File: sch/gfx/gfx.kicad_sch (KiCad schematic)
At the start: 104 parts

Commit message: schematic cleanups
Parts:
- removed R? (x2): 3k3, symbol AltDevice:R
- removed R?: 41k2, symbol AltDevice:R
- removed R?: 165k, symbol AltDevice:R
- removed U?: 74HC109, symbol AltDevice:74LS109
- removed U? (x2): 74HC02, symbol 74xx:74HC02
- removed U?: NE5532, symbol Amplifier_Operational:NE5532
- added C? (x3): 100n, symbol AltDevice:C
- added C?: 100u, symbol AltDevice:CP
- added C? (x2): 47u, symbol AltDevice:CP
- added D? (x2): 1N4148, symbol AltDevice:D
- added Q? (x2): 2N7000, symbol AltDevice:Q_NMOS_SGD
- added Q?: 2N3904, symbol AltDevice:Q_NPN_EBC
- added R5: 6k8, symbol AltDevice:R
- added R? (x2): 2k, symbol AltDevice:R
- added R?: 249k, symbol AltDevice:R
- added R?: 39, symbol AltDevice:R
- added R? (x4): 82k5, symbol AltDevice:R
- added R?: 499k, symbol AltDevice:R
- added RN?: 1k, Resistor_THT:R_Array_SIP9, symbol Device:R_Network08
- added unit 3 of U20
- added unit 4 of U6
- added unit 3 of U6
- D?: value 4148 -> 1N4148
- R?: Adjustment (none) -> HGAIN
- R?: Adjustment (none) -> VOFFSET
- R?: Adjustment (none) -> HOFFSET
- R?: Adjustment (none) -> VGAIN
- R?: value 1M -> 499k
- R?: value 1k -> 820
- R?: value 124k -> 249k
- RV?: renamed from R?; Adjustment (none) -> 4-6 SEP
- RV?: renamed from R?; Adjustment (none) -> FREQ
- RV?: renamed from R?; Adjustment (none) -> VSEP
- RV?: renamed from R?; Adjustment (none) -> 4-5 SEP
- U1: renamed from U?; value 74HC14 -> 'HC14; symbol 74xx:74HC14 -> AltDevice:74HC14
- U1: renamed from U?; value 74HC14 -> 'HC14
- U10: renamed from U?; value 74LS10 -> 'HC10
- U11, U12, U13, U9: renamed from U?; value 74HC161 -> 'HC161
- U14, U20, U7, U8: renamed from U?; value 74HC02 -> 'HC02
- U15: renamed from U?; value 74AHC244 -> 'AHC244
- U16, U17: renamed from U?; value 74HC273 -> 'HC273
- U2, U3, U4, U5: renamed from U?; value 74HC109 -> 'HC109
- U6: renamed from U?; value 74HC00 -> 'HC00
- gave numbers to parts that had none: 15
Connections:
- net +15V: now also C?.1, C?.1
- net +5V: now also U2.11 (S), U4.11 (S), U5.11 (S), C?.1, C?.1, Q?.3 (C), R?.2, R?.2, RN?.1 (common); no longer U2.5 (S), U4.5 (S), U4.5 (S), U5.5 (S)
- net -15V: now also C?.1, C?.2
- net CHAR0: now also U19.7 (A3); no longer U19.10 (A0)
- net CHAR1: now also U19.6 (A4); no longer U19.9 (A1)
- net CHAR2: now also U19.5 (A5); no longer U19.8 (A2)
- net CHAR3: now also U19.4 (A6); no longer U19.7 (A3)
- net CHAR4: now also U19.3 (A7); no longer U19.6 (A4)
- net CHAR5: now also U19.25 (A8); no longer U19.5 (A5)
- net CHARRSP0: now also RN?.2 (R1)
- net CHARRSP1: now also RN?.3 (R2)
- net CHARRSP2: now also RN?.4 (R3)
- net CHARRSP3: now also RN?.5 (R4)
- net CHARRSP4: now also RN?.6 (R5)
- net CHARRSP5: now also RN?.7 (R6)
- net CLK: now also U2.12 (C), U4.12 (C); no longer U2.4 (C), U4.4 (C)
- net DONE: now also U5.9 (Q); no longer U5.7 (Q)
- net DONEREQ: now also U7.5, U7.6; no longer U7.2, U7.3
- net GND: now also C?.1, C?.2, C?.2, C?.2, C?.2, C?.2, D?.2 (A), D?.2 (A), Q?.1 (S), Q?.1 (S), R5.1; no longer U14.3, U19.2 (A12)
- net HDOT0: now also U19.10 (A0), U6.5, R?.2; no longer R?.2, U19.4 (A6), U6.2
- net HDOT1: now also U19.9 (A1); no longer U19.3 (A7)
- net HDOT2: now also U19.8 (A2), U6.4; no longer U19.25 (A8), U6.1
- net LASTDOT: now also U8.4; no longer U8.1
- net LINE0: now also U19.21 (A10); no longer U19.24 (A9)
- net LINE1: now also U19.23 (A11); no longer U19.21 (A10)
- net LINE2: now also U19.2 (A12), R?.2; no longer U19.23 (A11)
- net POR: now also U2.9 (Q); no longer U2.7 (Q)
- net POS0: now also R?.2
- net POS2: now also R?.2, R?.2
- net POSCLK: now also U5.12 (C), R?.2; no longer U5.4 (C)
- net POSREQ0: now also U10.9; no longer U10.1
- net POSREQ1: now also U10.10; no longer U10.2
- net POSREQ2: now also U10.11; no longer U10.13
- net PREDONE: now also U14.12; no longer U14.3
- net RUN: now also U5.13 (K), U5.14 (J), U7.8; no longer U5.2 (J), U5.3 (K), U7.2
- net START: now also R5.2
- net ~DONE: now also U5.10 (Q); no longer U5.6 (Q)
- net ~LASTPOS: now also U10.8, U14.5, U14.6, U14.9; no longer U10.12
- net ~POR: now also U2.10 (Q), U4.15 (R); no longer U2.6 (Q), U4.1 (R), U4.1 (R)
- net ~RST: now also U1.6; no longer U1.2
- net ~RUN: now also U14.11, U20.6, U20.8; no longer U14.2, U20.2
- net V-: now reaches Q?.3 (C), R?.2
- net at C3.1, R?.1, R?.1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: now also D?.1 (K), R?.1, R?.1, R?.1, R?.1
- net at U12.10 (ENT): now also U14.4; no longer U14.1
- net at R4.2, U3.4 (C): now also U1.8; no longer U1.2
- net at U8.2: now also U6.6; no longer U6.3
- net H-: now reaches Q?.3 (C), R?.2
- net at C5.1, R?.1, R?.1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: now also D?.1 (K), R?.1, R?.1
- net at D?.1 (K), R3.2: now also U1.5; no longer U1.1
- net H+: now reaches Q?.3 (C), R?.1
- net at U13.10 (ENT): now also U14.10; no longer U14.1
- net at U7.3: now also U4.9 (Q); no longer U4.7 (Q)
- net at U20.1: now also U20.5; no longer U20.3
- net at C2.2, R2.1: now also U1.3; no longer U1.1
- net POSREQ'2: now reaches U15.14 (1Y2)
- net POSREQ'1: now reaches U15.16 (1Y1)
- net POSREQ'0: now reaches U15.18 (1Y0)
- net FLDREQ'0: now reaches U15.3 (2Y0)
- net FLDREQ'1: now reaches U15.5 (2Y1)
- net FLDREQ'2: now reaches U15.7 (2Y2)
- net at C?.1, RV?.1, RV?.2: now also U1.9; no longer U1.1
- net at U13.9 (~Pe): now also U14.13; no longer U14.1
- net V+: now reaches Q?.3 (C), R?.1
- net at R?.2: now also Q?.1 (E)
- removed net BLANK: U20.1
- net BRIGHT renamed ~INVERSE
- net ~INVERSE: now also U19.24 (A9)
- net BRIGHTRSP renamed ~INVRSP
- net ~INVRSP: now also RN?.8 (R7)
- net DIM renamed ~INTEN
- net ~INTEN: now also Q?.3 (D), U20.9
- net DIMRSP renamed ~INTENRSP
- net ~INTENRSP: now also RN?.9 (R8)
- net FIELD0 renamed FLD0
- net FIELD1 renamed FLD1
- net FIELD2 renamed FLD2
- net FLD2: now also Q?.2 (B)
- net FIELDREQ0 renamed FLDREQ0
- net FLDREQ0: now also U10.3; no longer U10.1
- net FIELDREQ1 renamed FLDREQ1
- net FLDREQ1: now also U10.4; no longer U10.2
- net FIELDREQ2 renamed FLDREQ2
- net FLDREQ2: now also U10.5; no longer U10.13
- removed net ~LASTFIELD: U10.12
- new net: R?.1, U6.11, U6.8
- new net: U6.10, U6.12, U6.13, U6.9, U8.1, U8.5, U8.6
- new net: U5.3 (K), U7.4, U7.9
- new net: U4.13 (K), U4.14 (J), U4.6 (Q)
- new net: Q?.2 (G), U20.4
- new net: R?.1, U1.10, U1.12
- new net: Q?.2 (G), U20.10
- new net: U1.11, U1.13, U3.6 (Q)
- new net: R?.1, R?.2 (x2)
- new net: U7.10, U7.11, U7.12
- new net: U5.15 (R), U7.13
- new net: U2.13 (K), U2.14 (J), U2.6 (Q)
- new net: U1.4, U2.1 (R), U2.15 (R)
- new net ~BLANK: Q?.3 (D)
- new net ~LASTFLD: U10.6, U14.8
- no-connect marks 12 -> 20
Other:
- note added: "0"
- note added: "0.5– 5mA"
- note added: "1"
- note added: "10µA"
- note added: "2"
- note added: "240µA"
- note added: "3"
- note added: "30µA"
- note added: "330µA"
- note added: "4"
- note added: "480µA"
- note added: "5"
- note added: "5µA"
- note added: "6"
- note added: "660µA"
- note added: "7"
- note added: "80µA"
- note added: "90µA"
- note added: "990µA"
- note added: "= virtual (B)lanking char, inserted for beam transit"
- note added: "B"
- note added: "HORIZONTAL DAC"
- note added: "J = START & DONE K = DONEREQ"
- note added: "OSD BUS"
- note added: "POSCLK lags CLK by one tP"
- note added: "Paper size is US Letter * 1.5, print scaled"
- note added: "SEQUENCE COUNTERS"
- note added: "Single cycle frame, START deasserted after fall of DONE"
- note added: "VERTICAL DAC"
- note removed: "(need to calculate)"
- note removed: "10µA per line 80µA per character box 0.5-5mA top-btm gap"
- note removed: "30µA per char"
- note removed: "5µA per dot"
- note removed: "Double flipflop stretches the transition to DONE, ensuring clean deactivation and reactivation."
- note removed: "FIELD4/5/6 SEPARATION"
- note removed: "GAP"
- note removed: "HOFFSET"
- note removed: "INTERFIELD BLANKING: In order to blank the beam while in transit between fields, a ninth virtual character is inserted at the end of every field. During this character, the beam is shut off. Due to the early increment of the field counter, this is simply visible to the external system as an extended prefetch of the first character of the next field."
- note removed: "J = START & !DONE K = DONEREQ"
- note removed: "POSCLK lags CLK by one tProp"
- note removed: "SYSTEM BUS"
- note removed: "Single cycle frame START deasserted after fall of DONE"
- note removed: "VGAIN"
- note removed: "VOFFSET"
- note removed: "dot = 5µA char width = 6; char = 30µA 8 chars per cell, cell = 240µA inter-cell space: 3 chars or 90µA cell with space: 330µA CELL0 CELL1 CELL2 CELL3 0µA 330µA 660µA 990µA 0µA 240µA480µA 990µA CELL4CELL5CELL6 CELL7"
- company: (none) -> Alexis Lockwood
- title: (none) -> OS2 On-screen display/graphics card

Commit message: Work in progress, not well organized, sorry
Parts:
- removed C?: 100p, symbol AltDevice:C
- removed R4: 6k8, symbol AltDevice:R
- removed R?: 39, symbol AltDevice:R
- removed RV?: 10k, symbol AltDevice:R_POT_TRIM
- removed unit 5 of U1
- removed unit 6 of U1
- removed U15: 'AHC244, symbol 74xx:74HC244
- removed U3: 'HC109, symbol AltDevice:74LS109
- removed U6: 'HC00, symbol 74xx:74HC00
- added R31: 499k, symbol AltDevice:R
- added R32: 249k, symbol AltDevice:R
- added U1: 1MHz, Oscillator:Oscillator_DIP-8, symbol Oscillator:CXO_DIP8
- added U15: 'AHC245, symbol 74xx:74LS245
- added unit 5 of U2
- added unit 6 of U2
- added unit 1 of U5
- added unit 1 of U6
- CD1: renamed from C?; value 100u -> 470µ
- CD2, CD41, CD44: renamed from C?; value 100n -> 1µ
- CD40, CD43: renamed from C?; value 47u -> 47µ
- R11, R12, R13, R14, R15: renamed from R?; value 82k5 -> 68k
- R28, R29, R43, R44: renamed from R?; symbol AltDevice:R -> AltDevice:R_HW
- R3: value 33k -> 10k
- R4: renamed from R?; value 39 -> 10
- U2: renamed from U1; symbol 74xx:74HC14 -> AltDevice:74HC14
- gave numbers to parts that had none: 45
- renumbered U14 to U10, U16 to U14, U17 to U16, U18 to U17, U19 to U18, U20 to U19, U1 to U2, U21 to U20, U22 to U21, U2 to U3, U9 to U4, U8 to U5, U10 to U6, U4 to U7, U5 to U8, U7 to U9
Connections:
- net +5V: now also U12.10 (ENT), U13.10 (ENT), U14.20 (VCC), U16.20 (VCC), U17.16 (VCC), U18.28 (VCC), U4.10 (ENT), U1.1 (EN), U1.8 (Vcc), U15.1 (A->B), U15.20 (VCC); no longer U12.7 (ENP), U13.7 (ENP), U4.7 (ENP)
- net CLK: now also U1.5 (OUT)
- net FLDREQ'0: now also U15.14 (B4)
- net FLDREQ'1: now also U15.13 (B5)
- net FLDREQ'2: now also U15.12 (B6)
- net FLDREQ0: now also U15.6 (A4)
- net FLDREQ1: now also U15.7 (A5)
- net FLDREQ2: now also U15.8 (A6)
- net GND: now also U14.10 (GND), U16.10 (GND), U17.8 (GND), U1.4 (GND), U15.10 (GND), U15.19 (CE), U15.5 (A3), U15.9 (A7)
- net HDOT0: now also U4.13 (Q1), U6.2; no longer U4.14 (Q0)
- net HDOT1: now also U4.12 (Q2), U5.9; no longer U4.13 (Q1), U5.3
- net HDOT2: now also U4.11 (Q3), U2.11, U2.13, U6.13; no longer U4.12 (Q2)
- net LASTDOT: now also U5.13; no longer U5.4
- net POR: now also U5.2
- net POSREQ'0: now also U15.18 (B0)
- net POSREQ'1: now also U15.17 (B1)
- net POSREQ'2: now also U15.16 (B2)
- net POSREQ0: now also U15.2 (A0)
- net POSREQ1: now also U15.3 (A1)
- net POSREQ2: now also U15.4 (A2)
- net RUN: no longer U4.10 (ENT)
- net ~POR: now also U7.1 (R); no longer U3.10 (Q)
- net ~RUN: now also U4.7 (ENP); no longer U10.11, U19.6, U19.8, U8.7 (Q)
- net at C5.1, D3.1 (K), R30.1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: now also R31.1, R32.1
- net at R4.1: now also U2.10, U2.12
- net at U10.4: now also U12.7 (ENP); no longer U12.10 (ENT)
- net RST#: now reaches U2.8
- net RST#: now also U11.1 (~MR), U12.1 (~MR), U13.1 (~MR), U4.1 (~MR)
- net at D1.2 (A), R3.1: now also U5.1
- net at U10.10: now also U13.7 (ENP); no longer U13.10 (ENT)
- net at U2.9: now also U2.6
- net DESCENDER0: now reaches U18.12 (D1)
- net DESCENDER0: now also R31.2
- net DESCENDER1: now reaches U18.13 (D2)
- net DESCENDER1: now also R32.2
- net ~BLANK renamed BLANK#
- net ~DONE renamed DONE#
- net ~INTEN renamed INTEN#
- net ~INTENRSP renamed INTENRSP#
- net ~INVERSE renamed CHAR6
- net ~INVRSP renamed CHARRSP6
- net ~LASTFLD renamed LASTFLD#
- net ~LASTPOS renamed LASTPOS#
- removed net ~RST: U11.1 (~MR), U12.1 (~MR), U13.1 (~MR), U2.6, U4.1 (~MR)
- new net: U4.14 (Q0), U6.1
- new net: U5.8, U6.12
- new net: U5.10, U5.11, U5.12
- new net POR#: U3.10 (Q)
- new net RUN#: U19.6, U19.8, U5.3, U8.7 (Q)
- no-connect marks 20 -> 17
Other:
- note added: "294µA"
- note added: "36µA"
- note added: "588µA"
- note added: "POSCLK lags CLK slightly"
- note added: "RST# lags CLK approximately 90°"
- note added: "hex: FNT1"
- note removed: "240µA"
- note removed: "480µA"
- note removed: "Adjust for fCLK = 500kHz (fosc = 1MHz)"
- note removed: "POSCLK lags CLK by one tP"
- note removed: "~RST~ lags CLK approximately 90°"

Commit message: blah blah
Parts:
- removed C4, C6: 100p, symbol AltDevice:C
- added R45, R46: 75, symbol AltDevice:R
- R24: value 5k1 -> 7k5
- R25, R30: value 2k -> 6k2
- R26, R41: value 150 -> 75
- R39: value 5k1 -> 3k
- RV4: value 10k -> 20k
- U14, U16: value 'HC273 -> 'AHCT273
- renumbered U22 to U21
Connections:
- net +15V: now also Q1.3 (C), R25.2, R30.2
- net +5V: now also R26.2, R41.2, R45.1, R46.1; no longer Q1.3 (C), R25.2, R30.2
- net GND: now also RV4.1, RV7.1, U21.3 (+), U21.5 (+); no longer U21.3 (+), U21.5 (+)
- net H-: now also R45.2; no longer R26.2
- net HDOT1: now also U5.6; no longer U5.9
- net LASTDOT: now also U5.1; no longer U5.13
- net POR: now also U5.11; no longer U5.2
- net RUN#: now also U10.11, U5.12; no longer U5.3
- net V-: now also R46.2; no longer R41.2
- net at Q7.2 (B): now also U21.1; no longer U21.7
- net at C5.1, D3.1 (K), R30.1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: now also R40.1, U21.6 (-); no longer RV5.3, U21.2 (-)
- net at D1.2 (A), R3.1: now also U5.13; no longer U5.1
- net at R38.2, R39.1: now also U21.2 (-); no longer U21.6 (-)
- net at R39.2, RV7.2: no longer RV7.1
- net at C5.2, Q6.2 (B): now also U21.7; no longer U21.1
- net at R24.2, RV4.2: no longer RV4.1
- net at U6.12: now also U5.5; no longer U5.8
- net at RV5.1, RV5.2: now also Q1.1 (E); no longer R40.1
- net at R40.2: now also RV5.3; no longer Q1.1 (E)
- new net: U5.2, U5.3, U5.4

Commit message: gfx board, pcb version
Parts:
- removed RN1: 1k, Resistor_THT:R_Array_SIP9, symbol Device:R_Network08
- added CD10, CD11, CD12, CD13, CD14, CD15, CD16, CD17, CD18, CD19, CD20, CD21, CD3, CD4, CD42, CD45, CD5, CD6, CD7, CD8, CD9: 1µ, Capacitor_SMD:C_0805_2012Metric_Pad1.15x1.40mm_HandSolder, symbol AltDevice:C
- added H1, H2: HOLE, MountingHole:MountingHole_3.2mm_M3_Pad_Via, symbol Connector:Conn_01x01_Male
- added P1: DIN41612_M_3x32, alt-libs:DIN41612_B_3x32_Horizontal, symbol AltConnector:DIN41612_M_3x32
- added RN1: 1k, Resistor_THT:R_Array_SIP10, symbol Device:R_Network09
- added unit 5 of U10
- added unit 5 of U19
- added unit 7 of U2
- added unit 3 of U20
- added unit 3 of U21
- added unit 3 of U3
- added unit 5 of U5
- added unit 4 of U6
- added unit 3 of U7
- added unit 3 of U8
- added unit 5 of U9
- C1, C2, C3, C5: footprint (none) -> Capacitor_THT:C_Disc_D4.7mm_W2.5mm_P5.00mm
- CD1: footprint (none) -> Capacitor_THT:CP_Radial_D8.0mm_P3.50mm; DKPN (none) -> 493-1743-ND
- CD2: footprint (none) -> Capacitor_SMD:C_0805_2012Metric_Pad1.15x1.40mm_HandSolder; Multiplier ×20 -> (none)
- CD40, CD43: footprint (none) -> Capacitor_THT:CP_Radial_D5.0mm_P2.00mm; DKPN (none) -> 493-1817-ND
- CD41, CD44: footprint (none) -> Capacitor_SMD:C_0805_2012Metric_Pad1.15x1.40mm_HandSolder; Multiplier ×2 -> (none)
- D1, D2, D3: footprint (none) -> Diode_THT:D_DO-35_SOD27_P10.16mm_Horizontal
- Q1, Q2, Q3, Q4, Q5, Q6, Q7: footprint (none) -> Package_TO_SOT_THT:TO-92
- R1, R10, R11, R12, R13, R14, R15, R16, R17, R18, R19, R2, R20, R21, R22, R23, R24, R25, R26, R27, R3, R30, R31, R32, R33, R34, R35, R36, R37, R38, R39, R4, R40, R41, R42, R45, R46, R5, R6, R7, R8, R9: footprint (none) -> Resistor_THT:R_Axial_DIN0207_L6.3mm_D2.5mm_P10.16mm_Horizontal
- R28, R29, R43, R44: footprint (none) -> Resistor_THT:R_Axial_DIN0309_L9.0mm_D3.2mm_P12.70mm_Horizontal
- RV1, RV2, RV3, RV4, RV5, RV6, RV7: footprint (none) -> alt-libs:stock_pot
- U10, U19, U2, U5, U6, U9: footprint (none) -> Package_DIP:DIP-14_W7.62mm
- U11, U12, U13, U3, U4, U7, U8: footprint (none) -> Package_DIP:DIP-16_W7.62mm
- U14, U15, U16: footprint (none) -> Package_DIP:DIP-20_W7.62mm
- U17: value 74HC237 -> 'HC237; footprint (none) -> Package_DIP:DIP-16_W7.62mm
- U18: footprint Package_DIP:DIP-28_W15.24mm -> Package_DIP:DIP-28_W15.24mm_Socket_LongPads
- U20, U21: footprint (none) -> Package_DIP:DIP-8_W7.62mm
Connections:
- net VCC is gone; now on net +5V: U11.16 (VCC), U12.16 (VCC), U13.16 (VCC), U4.16 (VCC)
- net ~RUN is gone; now on net RUN#: U4.7 (ENP)
- net +15V: now also CD42.1, P1.B28, U20.8 (V+), U21.8 (V+)
- net +5V: now also CD10.1, CD11.1, CD12.1, CD13.1, CD14.1, CD15.1, CD16.1, CD17.1, CD18.1, CD19.1, CD20.1, CD21.1, CD3.1, CD4.1, CD5.1, CD6.1, CD7.1, CD8.1, CD9.1, P1.A30, P1.A31, RN1.1 (common), U10.14 (VCC), U19.14 (VCC), U2.14 (VCC), U3.16 (VCC), U5.14 (VCC), U6.14 (VCC), U7.16 (VCC), U8.16 (VCC), U9.14 (VCC)
- net -15V: now also CD45.1, P1.B31, U20.4 (V-), U21.4 (V-)
- net GND: now also U21.3 (+), U21.5 (+), CD10.2, CD11.2, CD12.2, CD13.2, CD14.2, CD15.2, CD16.2, CD17.2, CD18.2, CD19.2, CD20.2, CD21.2, CD3.2, CD4.2, CD42.2, CD45.2, CD5.2, CD6.2, CD7.2, CD8.2, CD9.2, H1.1 (Pin_1), H2.1 (Pin_1), P1.A1, P1.A11, P1.A12, P1.A15, P1.A17, P1.A32, P1.A4, P1.A7, P1.A8, P1.B1, P1.B10, P1.B13, P1.B14, P1.B15, P1.B2, P1.B20, P1.B26, P1.B29, P1.B3, P1.B30, P1.B32, P1.B4, P1.B5, P1.B6, P1.B9, P1.C1, P1.C11, P1.C12, P1.C15, P1.C19, P1.C27, P1.C28, P1.C30, P1.C32, P1.C4, P1.C7, P1.C8, U10.7 (GND), U19.7 (GND), U2.7 (GND), U3.8 (GND), U5.7 (GND), U6.7 (GND), U7.8 (GND), U8.8 (GND), U9.7 (GND); no longer U21.3 (+), U21.5 (+)
- net INTEN#: no longer Q3.3 (D)
- net PREDONE: no longer R6.1, U10.2, U14.18 (D7)
- net at Q7.2 (B): now also U21.7; no longer U21.1
- net at C5.1, D3.1 (K), R30.1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: now also U21.2 (-); no longer U21.6 (-)
- net at R38.2, R39.1: now also U21.6 (-); no longer U21.2 (-)
- net at C5.2, Q6.2 (B): now also U21.1; no longer U21.7
- net BLANK# renamed A20
- net A20: now also P1.A20
- net CHARRSP0 renamed B22
- net B22: now also P1.B22, RN1.2 (R1)
- net CHARRSP1 renamed A22
- net A22: now also P1.A22, RN1.3 (R2)
- net CHARRSP2 renamed C23
- net C23: now also P1.C23, RN1.4 (R3)
- net CHARRSP3 renamed B23
- net B23: now also P1.B23, RN1.5 (R4)
- net CHARRSP4 renamed A23
- net A23: now also P1.A23, RN1.6 (R5)
- net CHARRSP5 renamed C24
- net C24: now also P1.C24, RN1.7 (R6)
- net CHARRSP6 renamed B24
- net B24: now also P1.B24, RN1.8 (R7)
- net DONE renamed A6
- net A6: now also P1.A6
- net FLDREQ'0 renamed B21
- net B21: now also P1.B21
- net FLDREQ'1 renamed A21
- net A21: now also P1.A21
- net FLDREQ'2 renamed C22
- net C22: now also P1.C22
- net H+ renamed A2
- net A2: now also P1.A2
- net H- renamed A3
- net A3: now also P1.A3
- net INTENRSP# renamed A24
- net A24: now also P1.A24, RN1.9 (R8)
- net POSREQ'0 renamed C25
- net C25: now also P1.C25
- net POSREQ'1 renamed B25
- net B25: now also P1.B25
- net POSREQ'2 renamed A25
- net A25: now also P1.A25
- net START renamed A5
- net A5: now also P1.A5
- net V+ renamed C2
- net C2: now also P1.C2
- net V- renamed C3
- net C3: now also P1.C3
- new net A10: P1.A10
- new net A13: P1.A13
- new net A14: P1.A14
- new net A16: P1.A16
- new net A18: P1.A18
- new net A19: P1.A19
- new net A26: P1.A26
- new net A27: P1.A27
- new net A28: P1.A28
- new net A29: P1.A29
- new net A9: P1.A9
- new net B11: P1.B11
- new net B12: P1.B12
- new net B16: P1.B16
- new net B17: P1.B17
- new net B18: P1.B18
- new net B19: P1.B19
- new net B27: P1.B27
- new net B7: P1.B7
- new net B8: P1.B8
- new net C10: P1.C10
- new net C13: P1.C13
- new net C14: P1.C14
- new net C16: P1.C16
- new net C17: P1.C17
- new net C18: P1.C18
- new net C20: P1.C20
- new net C21: P1.C21, Q3.3 (D)
- new net C26: P1.C26
- new net C29: P1.C29
- new net C31: P1.C31
- new net C5: P1.C5
- new net C6: P1.C6
- new net C9: P1.C9
- new net PREDONE': R6.1, U10.2, U14.18 (D7)
- no-connect marks 17 -> 18
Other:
- moved on the sheet: CD1, CD2, CD40, CD41, CD43, CD44

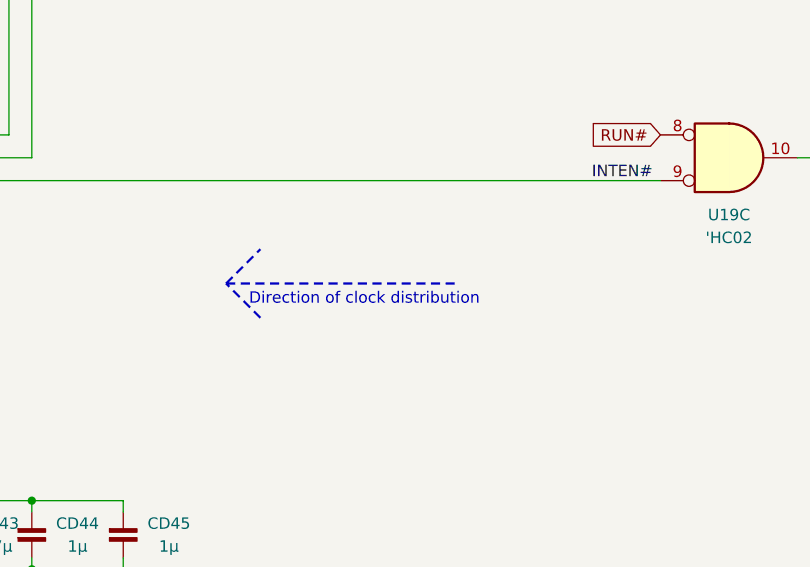
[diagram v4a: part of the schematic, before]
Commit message: gfx: sch adjustments and 3d models
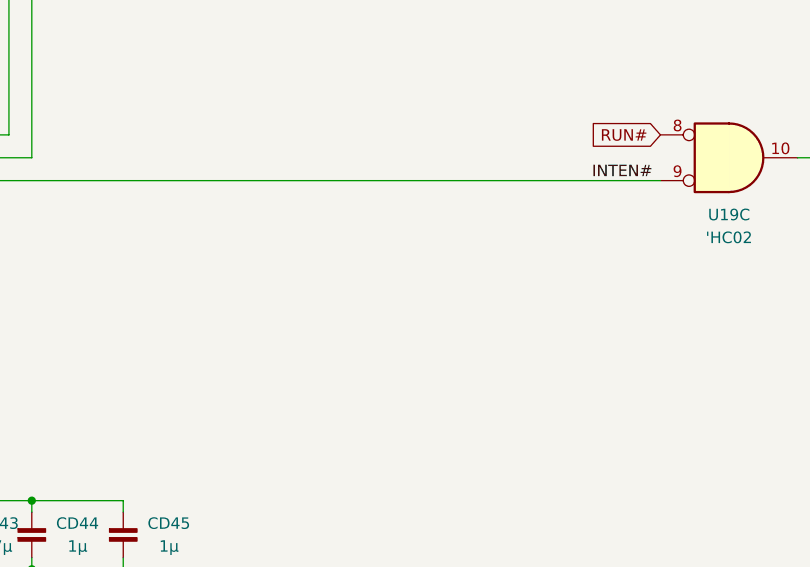
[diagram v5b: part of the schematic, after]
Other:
- note removed: "Direction of clock distribution"
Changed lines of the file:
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@@
-(kicad_sch (version 20200618) (host eeschema "(5.99.0-2039-g05a89863c)")
+(kicad_sch (version 20200618) (host eeschema "(5.99.0-2083-g40847c055)")
   (page 1 1)
   (paper "User" 419.1 323.85)
@@
   (junction (at 375.92 52.07) (diameter 0) (color 0 0 0 0))
   (junction (at 375.92 158.75) (diameter 0) (color 0 0 0 0))
-  (no_connect (at 264.16 99.06))
-  (no_connect (at 264.16 200.66))
-  (no_connect (at 151.13 205.74))
-  (no_connect (at 264.16 205.74))
-  (no_connect (at 264.16 88.9))
-  (no_connect (at 264.16 203.2))
+  (no_connect (at 88.9 231.14))
+  (no_connect (at 76.2 113.03))
+  (no_connect (at 53.34 118.11))
   (no_connect (at 99.06 246.38))
-  (no_connect (at 264.16 198.12))
   (no_connect (at 264.16 208.28))
-  (no_connect (at 76.2 113.03))
   (no_connect (at 64.77 35.56))
-  (no_connect (at 53.34 118.11))
-  (no_connect (at 88.9 231.14))
+  (no_connect (at 198.12 193.04))
+  (no_connect (at 264.16 198.12))
+  (no_connect (at 264.16 205.74))
+  (no_connect (at 151.13 205.74))
+  (no_connect (at 264.16 99.06))
+  (no_connect (at 88.9 182.88))
+  (no_connect (at 264.16 88.9))
+  (no_connect (at 264.16 200.66))
   (no_connect (at 137.16 43.18))
   (no_connect (at 88.9 214.63))
-  (no_connect (at 88.9 182.88))
   (no_connect (at 151.13 215.9))
-  (no_connect (at 198.12 193.04))
+  (no_connect (at 264.16 203.2))
   (wire (pts (xy 16.51 297.18) (xy 16.51 298.45))
     (stroke (width 0) (type solid) (color 0 0 0 0))
@@
     (stroke (width 0.1524) (type dot) (color 187 0 255 1))
   )
-  (polyline (pts (xy 299.72 274.32) (xy 303.53 270.51))
-    (stroke (width 0.254) (type dash) (color 255 0 255 1))
-  )
-  (polyline (pts (xy 299.72 274.32) (xy 325.12 274.32))
-    (stroke (width 0.254) (type dash) (color 255 0 255 1))
-  )
-  (polyline (pts (xy 303.53 278.13) (xy 299.72 274.32))
-    (stroke (width 0.254) (type dash) (color 255 0 255 1))
-  )
   (polyline (pts (xy 317.5 78.74) (xy 317.5 104.14))
     (stroke (width 0.0001) (type dash_dot) (color 0 0 0 0))
@@
     (effects (font (size 1.27 1.27)) (justify right bottom))
   )
-  (text "Direction of clock distribution" (at 302.26 276.86 0)
-    (effects (font (size 1.27 1.27)) (justify left bottom))
-  )
   (text "0" (at 318.77 82.296 0)
